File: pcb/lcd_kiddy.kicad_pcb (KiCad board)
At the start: 2 copper layers, 47 x 72 mm, 4 parts, among them J1 CONN_02X08, J3 BARREL_JACK, U1 ATMEGA168A-PU

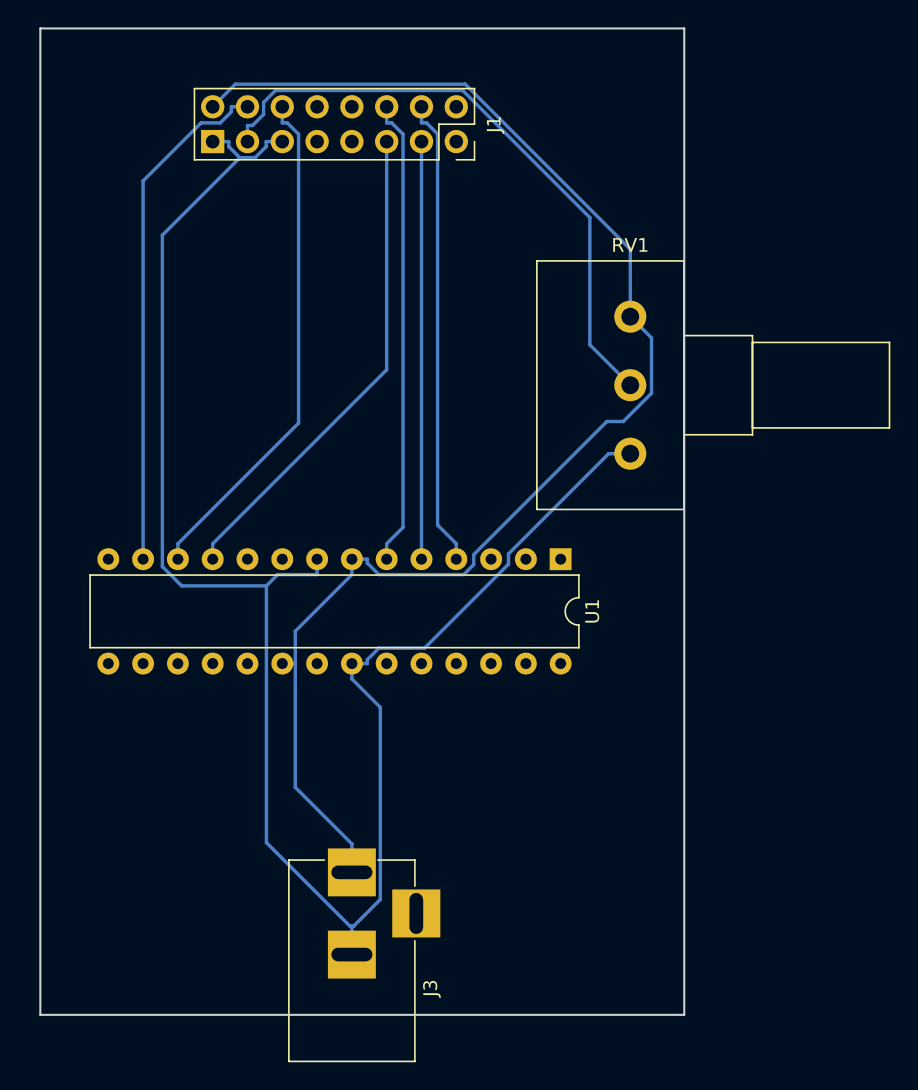
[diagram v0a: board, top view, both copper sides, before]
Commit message: PD6-7を LCDの制御PIN(R/W, RS)に割り当てていたため，PINの割当を大幅に変更。
  要するに，大改造。
bread boardの配線で検証できていなければならない問題であったと反省。

変更が必要となった理由。
  LCDの制御を4bit modeで行う。この場合，P?7-4のいずれかをLCDの制御PINに
割り当ててしまうとChaN氏のlibraryを使えない。
  何故ならば，P?7-4はChaN氏のlibraryの4bit modeにおいて，
任意のdataを書き込むために使用するから。

  PIN assign が腐っており，かつ，配線の修正が不可能でどうしてもsoft側で
配線を任意に変更しなければならない場合に備えて，
firmware/shuffle_8bits.c
を書いた。
  shuffle_8bits を使用すれば，script kiddy から取ってきた，
"kiddy" を表現できるとは思う。しかし，lcd-kiddyでは， 設計の甘さを原因とする
複雑怪奇な配線を許容しない。autorouter＆PCBによって複雑怪奇な配線の基板を
作成する事は対処療法的な解決であり，下手糞な対策である。

  根治療法を是非とする。

やれやれ，基板の作り直しか。
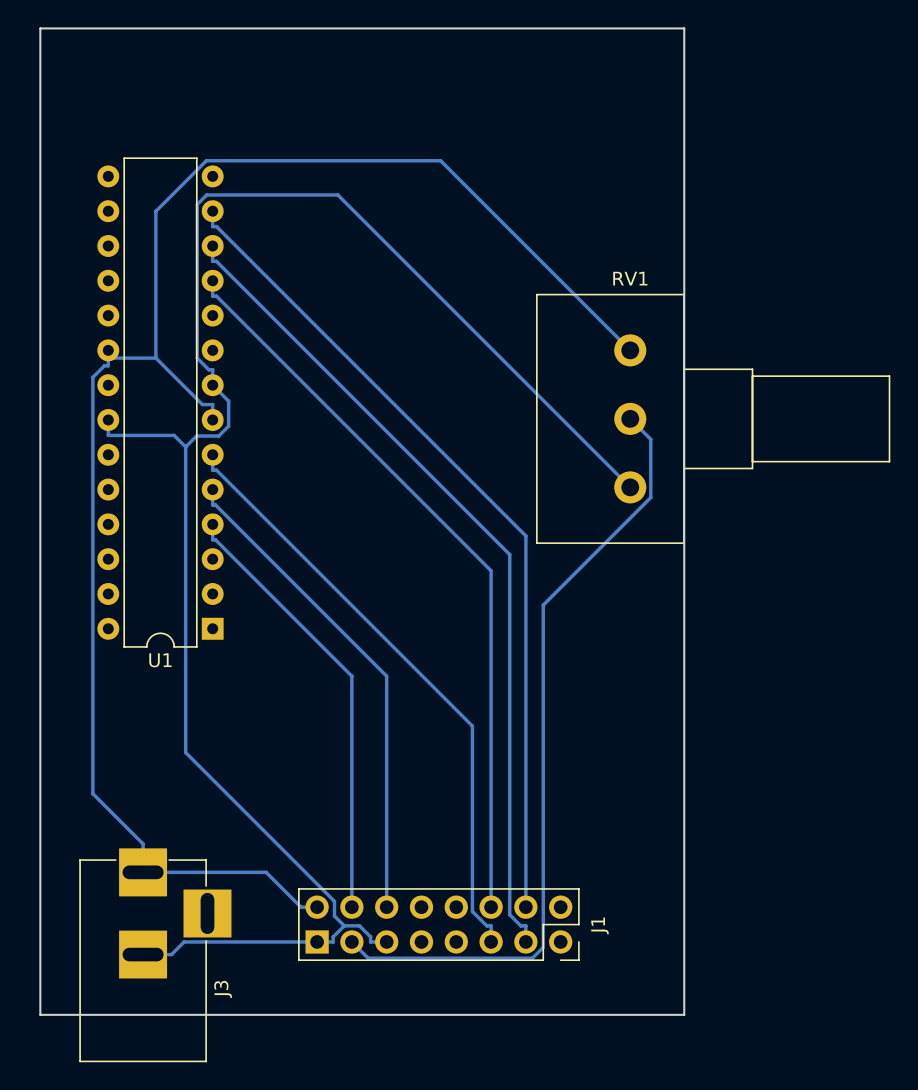
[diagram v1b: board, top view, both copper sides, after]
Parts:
- moved J1 58.9 mm to (147.3, 177.8)
- moved U1 25.9 mm to (121.9, 154.9), turned to 180 degrees
- moved J3 15.2 mm to (116.8, 172.7)
- moved RV1 2.46 mm to (152.4, 144.6)
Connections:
- J1 pad 11: /PD5 -> /PD4
- J1 pad 12: /PD4 -> /PD5
- J1 pad 13: /PD3 -> /PD6
- J1 pad 14: /PD2 -> /PD7
- J1 pad 4: /PD7 -> /PD2
- J1 pad 6: /PD6 -> /PD3
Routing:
- net /PD6: track 37.4 -> 60.6 mm
- net /PD7: track 37.7 -> 60.4 mm
- net /PD5: track 35.7 -> 54.3 mm
- net +5V: track 102.9 -> 116.8 mm
- net Net-(J1-Pad3): track 45.0 -> 57.2 mm
- net /PD4: track 34.2 -> 44.3 mm
- net /PD3: track 30.5 -> 35.9 mm
- net /PD2: track 34.3 -> 32.3 mm
- net GND: track 129.8 -> 128.2 mm

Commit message: PD4-7を4bit busに，PD3->E, PD2->RSの制御に割り当てた。
ChaN氏の図示する配線と同じにしたつもり。
http://elm-chan.org/fsw/ezlcd/00index_j.html
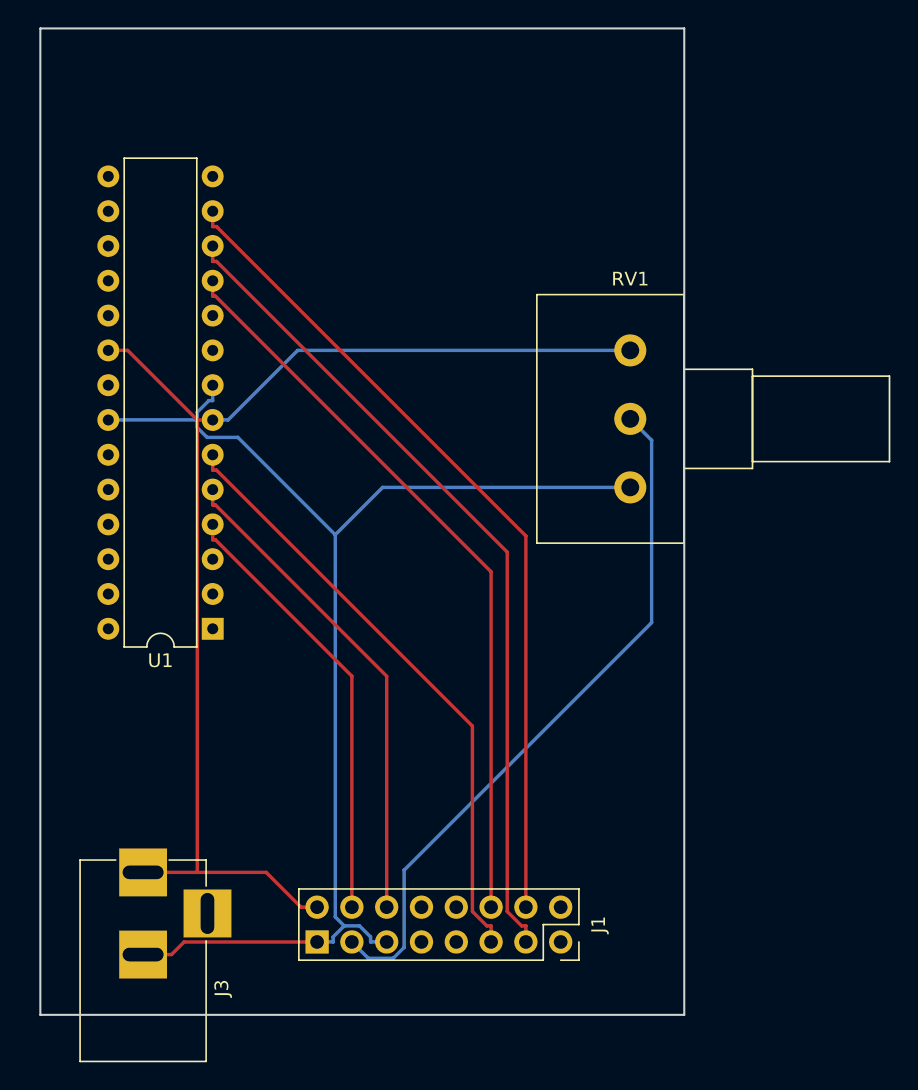
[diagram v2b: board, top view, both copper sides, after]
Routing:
- net GND: track 128.2 -> 94.9 mm
- net +5V: track 116.8 -> 89.1 mm
- net Net-(J1-Pad3): track 57.2 -> 51.3 mm

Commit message: LCDの表示部が基板の上空を通過するよう部品の配置を修正。付随して配線も修正。
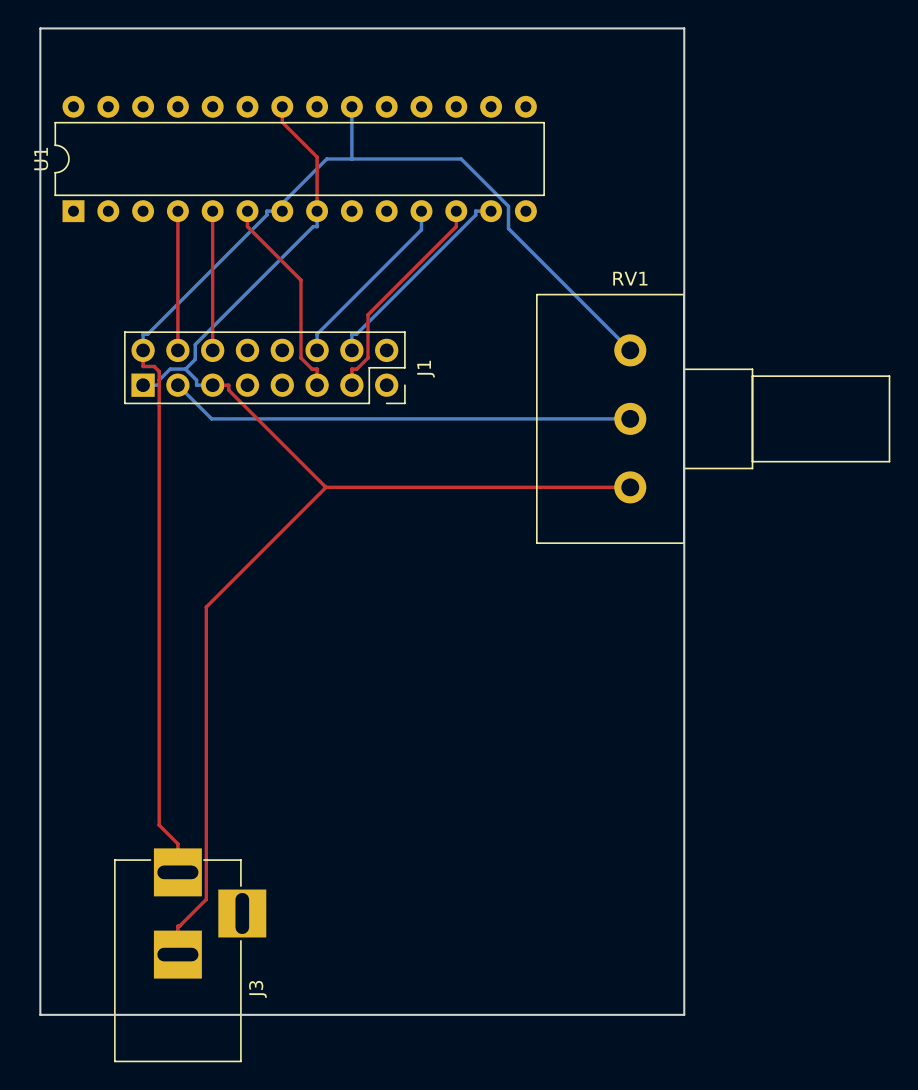
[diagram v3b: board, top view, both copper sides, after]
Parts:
- moved J1 42.6 mm to (134.6, 137.2)
- moved U1 32.1 mm to (111.8, 124.5), turned to 90 degrees
- moved J3 2.54 mm to (119.4, 172.7)
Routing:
- net /PD7: track 60.4 -> 15.2 mm
- net /PD6: track 60.6 -> 16.1 mm
- net /PD5: track 54.3 -> 13.3 mm
- net /PD4: track 44.3 -> 15.0 mm
- net /PD3: track 35.9 -> 10.2 mm
- net /PD2: track 32.3 -> 10.2 mm
- net Net-(J1-Pad3): track 51.3 -> 34.0 mm
- net GND: track 94.9 -> 103.3 mm
- net +5V: track 89.1 -> 92.9 mm

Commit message: 部品を上部にまとめた完成版。部品の干渉がないよう配置を工夫した。
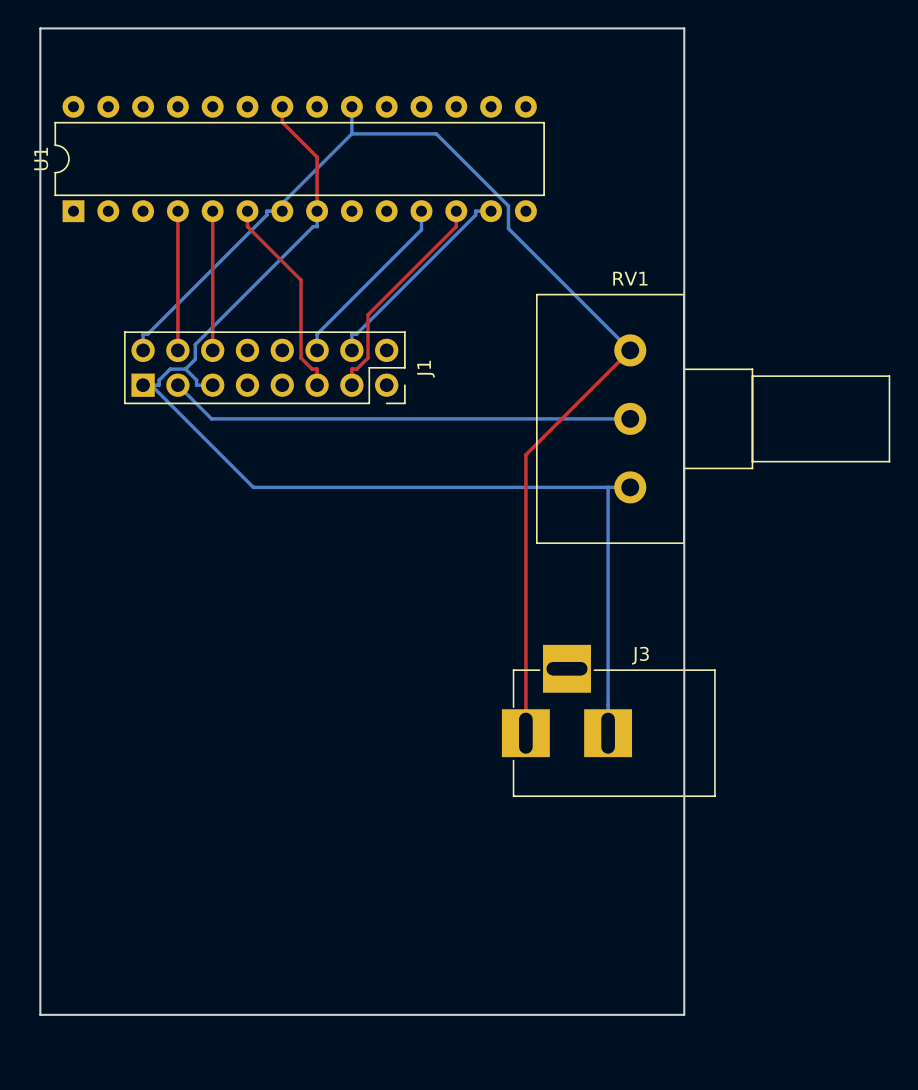
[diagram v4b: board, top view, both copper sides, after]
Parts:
- moved J3 27.4 mm to (144.8, 162.6), turned to 180 degrees
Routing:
- net GND: track 103.3 -> 86.8 mm
- net +5V: track 92.9 -> 84.1 mm
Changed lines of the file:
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@@
     (links 16)
     (no_connects 0)
-    (area 109.264999 111.044999 171.675001 186.945001)
+    (area 108.455 111.044999 171.675001 186.945001)
     (thickness 1.6)
     (drawings 4)
-    (tracks 67)
+    (tracks 59)
     (zones 0)
     (modules 4)
@@
   )
   (module Connectors:BARREL_JACK (layer F.Cu)
-    (at 119.38 172.72 90)
+    (at 144.78 162.56 180)
     (descr "DC Barrel Jack")
     (tags "Power Jack")
-    (fp_text reference J3 (at -8.45 5.75 270) (layer F.SilkS)
-      (effects (font (size 1 1) (thickness 0.15)))
-    )
-    (fp_text value BARREL_JACK (at -6.2 -5.5 90) (layer F.Fab)
+    (fp_text reference J3 (at -8.45 5.75 360) (layer F.SilkS)
+      (effects (font (size 1 1) (thickness 0.15)))
+    )
+    (fp_text value BARREL_JACK (at -6.2 -5.5 180) (layer F.Fab)
       (effects (font (size 1 1) (thickness 0.15)))
     )
@@
     (fp_line (start 0.8 4.5) (end 0.8 -4.5) (layer F.Fab) (width 0.1))
     (fp_line (start 0.8 -4.5) (end -13.7 -4.5) (layer F.Fab) (width 0.1))
-    (pad 1 thru_hole rect (at 0 0 90) (size 3.5 3.5) (drill oval 1 3) (layers *.Cu *.Mask)
-      (net 2 +5V))
-    (pad 2 thru_hole rect (at -6 0 90) (size 3.5 3.5) (drill oval 1 3) (layers *.Cu *.Mask)
-      (net 1 GND))
-    (pad 3 thru_hole rect (at -3 4.7 90) (size 3.5 3.5) (drill oval 3 1) (layers *.Cu *.Mask))
+    (pad 1 thru_hole rect (at 0 0 180) (size 3.5 3.5) (drill oval 1 3) (layers *.Cu *.Mask)
+      (net 2 +5V))
+    (pad 2 thru_hole rect (at -6 0 180) (size 3.5 3.5) (drill oval 1 3) (layers *.Cu *.Mask)
+      (net 1 GND))
+    (pad 3 thru_hole rect (at -3 4.7 180) (size 3.5 3.5) (drill oval 3 1) (layers *.Cu *.Mask))
   )
   (module Connector_PinSocket_2.54mm:PinSocket_2x08_P2.54mm_Vertical_R (layer F.Cu)
@@
   (segment (start 127 117.9653) (end 129.54 120.5053) (width 0.25) (layer F.Cu) (net 1))
   (segment (start 127 116.84) (end 127 117.9653) (width 0.25) (layer F.Cu) (net 1))
-  (segment (start 116.84 137.16) (end 118.0153 137.16) (width 0.25) (layer B.Cu) (net 1))
-  (segment (start 121.92 137.16) (end 123.0953 137.16) (width 0.25) (layer F.Cu) (net 1))
-  (segment (start 121.4553 153.3527) (end 130.188 144.62) (width 0.25) (layer F.Cu) (net 1))
-  (segment (start 121.4553 174.6992) (end 121.4553 153.3527) (width 0.25) (layer F.Cu) (net 1))
-  (segment (start 119.5098 176.6447) (end 121.4553 174.6992) (width 0.25) (layer F.Cu) (net 1))
-  (segment (start 119.38 176.6447) (end 119.5098 176.6447) (width 0.25) (layer F.Cu) (net 1))
-  (segment (start 123.0953 137.5273) (end 130.188 144.62) (width 0.25) (layer F.Cu) (net 1))
-  (segment (start 123.0953 137.16) (end 123.0953 137.5273) (width 0.25) (layer F.Cu) (net 1))
-  (segment (start 130.188 144.62) (end 152.4 144.62) (width 0.25) (layer F.Cu) (net 1))
-  (segment (start 119.38 178.72) (end 119.38 176.6447) (width 0.25) (layer F.Cu) (net 1))
+  (segment (start 116.84 137.16) (end 117.4277 137.16) (width 0.25) (layer B.Cu) (net 1))
+  (segment (start 117.4277 137.16) (end 118.0153 137.16) (width 0.25) (layer B.Cu) (net 1))
+  (segment (start 150.78 162.56) (end 150.78 160.4847) (width 0.25) (layer B.Cu) (net 1))
+  (segment (start 150.78 144.62) (end 150.78 160.4847) (width 0.25) (layer B.Cu) (net 1))
+  (segment (start 124.8877 144.62) (end 150.78 144.62) (width 0.25) (layer B.Cu) (net 1))
+  (segment (start 117.4277 137.16) (end 124.8877 144.62) (width 0.25) (layer B.Cu) (net 1))
+  (segment (start 150.78 144.62) (end 152.4 144.62) (width 0.25) (layer B.Cu) (net 1))
   (segment (start 125.8747 124.7413) (end 125.8747 124.46) (width 0.25) (layer B.Cu) (net 2))
   (segment (start 117.1713 133.4447) (end 125.8747 124.7413) (width 0.25) (layer B.Cu) (net 2))
   (segment (start 116.84 133.4447) (end 117.1713 133.4447) (width 0.25) (layer B.Cu) (net 2))
   (segment (start 116.84 134.62) (end 116.84 133.4447) (width 0.25) (layer B.Cu) (net 2))
-  (segment (start 117.6481 135.7953) (end 116.84 135.7953) (width 0.25) (layer F.Cu) (net 2))
-  (segment (start 118.0153 136.1625) (end 117.6481 135.7953) (width 0.25) (layer F.Cu) (net 2))
-  (segment (start 118.0153 169.28) (end 118.0153 136.1625) (width 0.25) (layer F.Cu) (net 2))
-  (segment (start 119.38 170.6447) (end 118.0153 169.28) (width 0.25) (layer F.Cu) (net 2))
-  (segment (start 119.38 172.72) (end 119.38 170.6447) (width 0.25) (layer F.Cu) (net 2))
-  (segment (start 116.84 134.62) (end 116.84 135.7953) (width 0.25) (layer F.Cu) (net 2))
+  (segment (start 144.78 142.24) (end 152.4 134.62) (width 0.25) (layer F.Cu) (net 2))
+  (segment (start 144.78 162.56) (end 144.78 142.24) (width 0.25) (layer F.Cu) (net 2))
   (segment (start 127 124.46) (end 126.4374 124.46) (width 0.25) (layer B.Cu) (net 2))
   (segment (start 126.4374 124.46) (end 125.8747 124.46) (width 0.25) (layer B.Cu) (net 2))
-  (segment (start 132.08 120.65) (end 132.08 116.84) (width 0.25) (layer B.Cu) (net 2))
-  (segment (start 130.2474 120.65) (end 132.08 120.65) (width 0.25) (layer B.Cu) (net 2))
-  (segment (start 126.4374 124.46) (end 130.2474 120.65) (width 0.25) (layer B.Cu) (net 2))
-  (segment (start 143.51 125.73) (end 152.4 134.62) (width 0.25) (layer B.Cu) (net 2))
-  (segment (start 143.51 124.0976) (end 143.51 125.73) (width 0.25) (layer B.Cu) (net 2))
-  (segment (start 140.0624 120.65) (end 143.51 124.0976) (width 0.25) (layer B.Cu) (net 2))
-  (segment (start 132.08 120.65) (end 140.0624 120.65) (width 0.25) (layer B.Cu) (net 2))
+  (segment (start 138.2442 118.8174) (end 132.08 118.8174) (width 0.25) (layer B.Cu) (net 2))
+  (segment (start 143.51 124.0832) (end 138.2442 118.8174) (width 0.25) (layer B.Cu) (net 2))
+  (segment (start 143.51 125.73) (end 143.51 124.0832) (width 0.25) (layer B.Cu) (net 2))
+  (segment (start 152.4 134.62) (end 143.51 125.73) (width 0.25) (layer B.Cu) (net 2))
+  (segment (start 126.4374 124.46) (end 132.08 118.8174) (width 0.25) (layer B.Cu) (net 2))
+  (segment (start 132.08 118.8174) (end 132.08 116.84) (width 0.25) (layer B.Cu) (net 2))
   (segment (start 121.84 139.62) (end 119.38 137.16) (width 0.25) (layer B.Cu) (net 3))
   (segment (start 152.4 139.62) (end 121.84 139.62) (width 0.25) (layer B.Cu) (net 3))
